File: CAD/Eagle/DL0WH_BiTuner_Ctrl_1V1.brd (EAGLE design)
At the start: 96.5 x 73 mm, 141 parts, among them Q0321 ABS07-32.768KHZ, U0101 STM32L476RXT_64PIN_LDO, U0601 MC33996, U0701 MC33996, U0801 MC33996, U0921 TS5A23166, U0951 OPA354, U1001 MAX232_SOIC16, U1101 MAX232_SOIC16, U1201 LM53603-Q1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

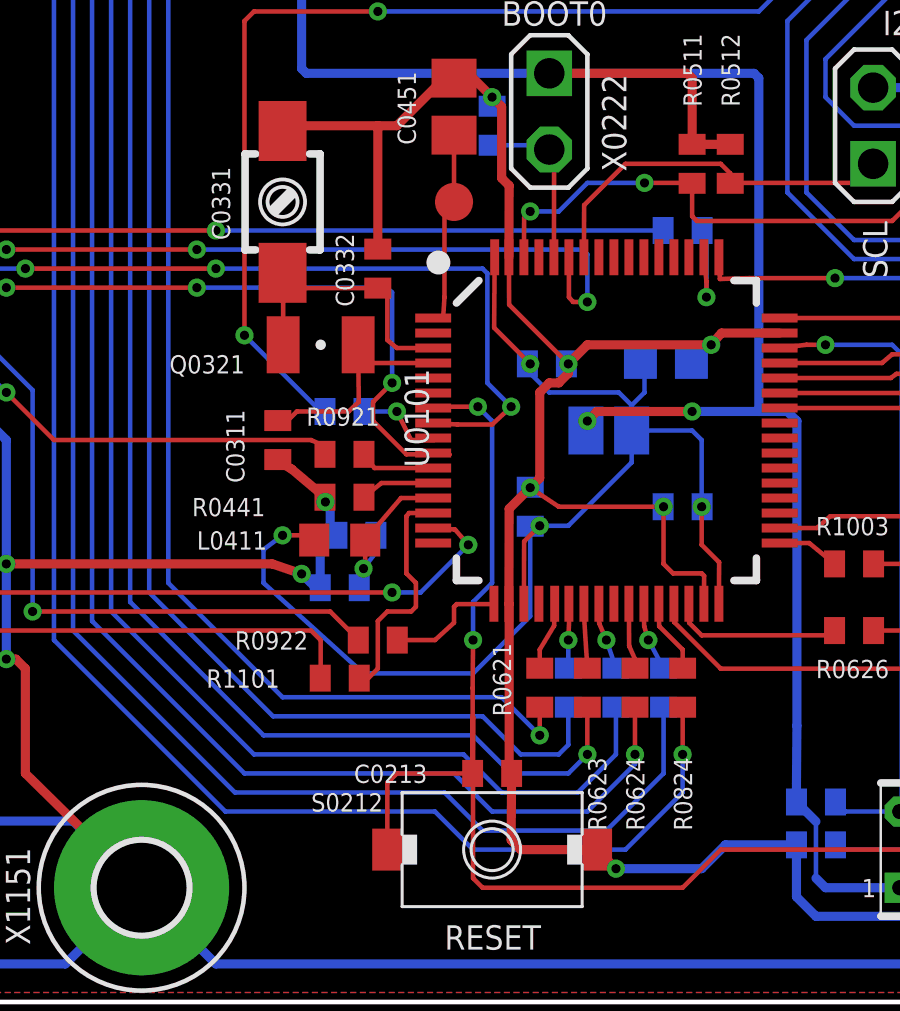
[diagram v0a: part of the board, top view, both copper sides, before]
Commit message: HW_1V1 - CAD/Eagle - after DRC fixes, ready for production with new STM32L476 device package.
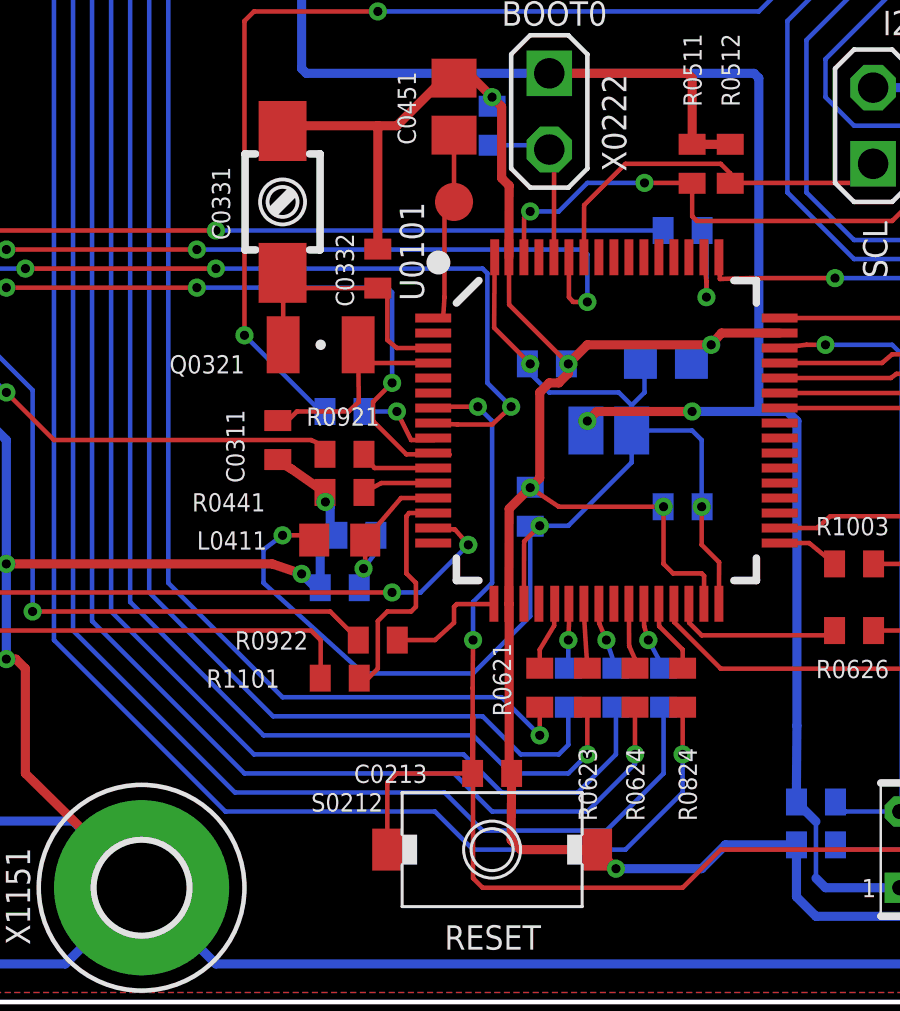
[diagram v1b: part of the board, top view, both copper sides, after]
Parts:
- moved R0441 0.16 mm to (59.8, 17.0)
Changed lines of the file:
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@@
 <layer number="37" name="tTest" color="7" fill="1" visible="no" active="yes"/>
 <layer number="38" name="bTest" color="7" fill="1" visible="no" active="yes"/>
-<layer number="39" name="tKeepout" color="4" fill="11" visible="no" active="yes"/>
-<layer number="40" name="bKeepout" color="1" fill="11" visible="no" active="yes"/>
-<layer number="41" name="tRestrict" color="4" fill="10" visible="no" active="yes"/>
-<layer number="42" name="bRestrict" color="1" fill="10" visible="no" active="yes"/>
-<layer number="43" name="vRestrict" color="2" fill="10" visible="no" active="yes"/>
+<layer number="39" name="tKeepout" color="4" fill="11" visible="yes" active="yes"/>
+<layer number="40" name="bKeepout" color="1" fill="11" visible="yes" active="yes"/>
+<layer number="41" name="tRestrict" color="4" fill="10" visible="yes" active="yes"/>
+<layer number="42" name="bRestrict" color="1" fill="10" visible="yes" active="yes"/>
+<layer number="43" name="vRestrict" color="2" fill="10" visible="yes" active="yes"/>
 <layer number="44" name="Drills" color="7" fill="1" visible="no" active="yes"/>
 <layer number="45" name="Holes" color="7" fill="1" visible="yes" active="yes"/>
@@
 <layer number="49" name="Reference" color="7" fill="1" visible="no" active="yes"/>
 <layer number="50" name="dxf" color="7" fill="1" visible="no" active="no"/>
-<layer number="51" name="tDocu" color="14" fill="1" visible="yes" active="yes"/>
-<layer number="52" name="bDocu" color="6" fill="1" visible="yes" active="yes"/>
+<layer number="51" name="tDocu" color="14" fill="1" visible="no" active="yes"/>
+<layer number="52" name="bDocu" color="6" fill="1" visible="no" active="yes"/>
 <layer number="53" name="tGND_GNDA" color="7" fill="9" visible="no" active="no"/>
 <layer number="54" name="bGND_GNDA" color="1" fill="9" visible="no" active="no"/>
@@
 <attribute name="VALUE" x="64.135" y="5.715" size="0.6096" layer="27" font="vector" ratio="10"/>
 </element>
-<element name="R0441" library="df4iah_rcl" package="R0402" value="0R" x="59.84875" y="16.8275" smashed="yes">
-<attribute name="NAME" x="54.76875" y="16.1925" size="0.6096" layer="25" font="vector" ratio="10"/>
-<attribute name="VALUE" x="59.21375" y="14.9225" size="0.6096" layer="27" font="vector" ratio="10"/>
+<element name="R0441" library="df4iah_rcl" package="R0402" value="0R" x="59.84875" y="16.98625" smashed="yes">
+<attribute name="NAME" x="54.76875" y="16.35125" size="0.6096" layer="25" font="vector" ratio="10"/>
+<attribute name="VALUE" x="59.21375" y="15.08125" size="0.6096" layer="27" font="vector" ratio="10"/>
 </element>
 <element name="C0451" library="df4iah_rcl" package="C0805" value="47uF" x="63.5" y="29.845" smashed="yes" rot="R90">
@@
 </element>
 <element name="U0101" library="df4iah_stm32l4" package="LQFP64" value="STM32L476RXT_64PIN_LDO" x="68.58" y="19.05" smashed="yes">
-<attribute name="NAME" x="62.6625" y="17.82125" size="0.8128" layer="25" rot="R90"/>
+<attribute name="NAME" x="62.50375" y="23.3775" size="0.8128" layer="25" rot="R90"/>
 <attribute name="VALUE" x="65.555" y="16.6" size="0.8128" layer="27"/>
 </element>
@@
 </element>
 <element name="R0622" library="df4iah_rcl" package="R0402" value="0R" x="67.31" y="10.4775" smashed="yes" rot="MR270">
-<attribute name="NAME" x="66.9925" y="5.715" size="0.6096" layer="26" font="vector" ratio="10" rot="MR90"/>
+<attribute name="NAME" x="66.83375" y="6.0325" size="0.6096" layer="26" font="vector" ratio="10" rot="MR90"/>
 <attribute name="VALUE" x="68.8975" y="12.065" size="0.6096" layer="28" font="vector" ratio="10" rot="MR270"/>
 </element>
 <element name="R0623" library="df4iah_rcl" package="R0402" value="47R" x="67.945" y="10.4775" smashed="yes" rot="R270">
-<attribute name="NAME" x="68.58" y="5.715" size="0.6096" layer="25" font="vector" ratio="10" rot="R90"/>
+<attribute name="NAME" x="68.2625" y="6.0325" size="0.6096" layer="25" font="vector" ratio="10" rot="R90"/>
 <attribute name="VALUE" x="66.3575" y="12.065" size="0.6096" layer="27" font="vector" ratio="10" rot="R270"/>
 </element>
 <element name="R0624" library="df4iah_rcl" package="R0402" value="47R" x="69.5325" y="10.4775" smashed="yes" rot="R270">
-<attribute name="NAME" x="69.85" y="5.715" size="0.6096" layer="25" font="vector" ratio="10" rot="R90"/>
+<attribute name="NAME" x="69.85" y="6.0325" size="0.6096" layer="25" font="vector" ratio="10" rot="R90"/>
 <attribute name="VALUE" x="67.945" y="12.065" size="0.6096" layer="27" font="vector" ratio="10" rot="R270"/>
 </element>
 <element name="R0625" library="df4iah_rcl" package="R0402" value="47R" x="68.8975" y="10.4775" smashed="yes" rot="MR270">
-<attribute name="NAME" x="68.58" y="5.715" size="0.6096" layer="26" font="vector" ratio="10" rot="MR90"/>
+<attribute name="NAME" x="68.58" y="6.0325" size="0.6096" layer="26" font="vector" ratio="10" rot="MR90"/>
 <attribute name="VALUE" x="70.485" y="12.065" size="0.6096" layer="28" font="vector" ratio="10" rot="MR270"/>
 </element>
@@
 </element>
 <element name="R0724" library="df4iah_rcl" package="R0402" value="47R" x="70.485" y="10.4775" smashed="yes" rot="MR270">
-<attribute name="NAME" x="70.1675" y="5.715" size="0.6096" layer="26" font="vector" ratio="10" rot="MR90"/>
+<attribute name="NAME" x="70.1675" y="6.0325" size="0.6096" layer="26" font="vector" ratio="10" rot="MR90"/>
 <attribute name="VALUE" x="72.0725" y="12.065" size="0.6096" layer="28" font="vector" ratio="10" rot="MR270"/>
 </element>
 <element name="R0824" library="df4iah_rcl" package="R0402" value="47R" x="71.12" y="10.4775" smashed="yes" rot="R270">
-<attribute name="NAME" x="71.4375" y="5.715" size="0.6096" layer="25" font="vector" ratio="10" rot="R90"/>
+<attribute name="NAME" x="71.59625" y="6.0325" size="0.6096" layer="25" font="vector" ratio="10" rot="R90"/>
 <attribute name="VALUE" x="69.5325" y="12.065" size="0.6096" layer="27" font="vector" ratio="10" rot="R270"/>
 </element>
@@
 <wire x1="65.3375" y1="13.2675" x2="65.3375" y2="7.855" width="0.3048" layer="1"/>
 <wire x1="65.3375" y1="7.855" x2="65.42" y2="7.62" width="0.3048" layer="1"/>
-<wire x1="59.19875" y1="16.8275" x2="58.0875" y2="17.765" width="0.3048" layer="1"/>
+<wire x1="59.19875" y1="16.98625" x2="58.0875" y2="17.765" width="0.3048" layer="1"/>
 <wire x1="58.0875" y1="17.765" x2="57.785" y2="17.93875" width="0.3048" layer="1"/>
 <wire x1="57.785" y1="17.93875" x2="57.61125" y2="18.0975" width="0.1524" layer="1"/>
@@
 <wire x1="67.945" y1="21.9075" x2="72.0725" y2="21.9075" width="0.3048" layer="1"/>
 <via x="59.21375" y="16.66875" extent="1-16" drill="0.3048"/>
-<wire x1="59.19875" y1="16.8275" x2="59.055" y2="16.66875" width="0.1524" layer="1"/>
+<wire x1="59.19875" y1="16.98625" x2="59.055" y2="16.66875" width="0.1524" layer="1"/>
 <wire x1="59.055" y1="16.66875" x2="59.21375" y2="16.66875" width="0.3048" layer="1"/>
 <wire x1="59.595625" y1="15.5575" x2="59.3725" y2="15.5575" width="0.3048" layer="16"/>
@@
 <contactref element="U0101" pad="12"/>
 <wire x1="62.805" y1="17.3" x2="61.08" y2="17.3" width="0.1524" layer="1"/>
-<wire x1="61.08" y1="17.3" x2="60.49875" y2="16.8275" width="0.1524" layer="1"/>
+<wire x1="61.08" y1="17.3" x2="60.49875" y2="16.98625" width="0.1524" layer="1"/>
 </signal>
 <signal name="PH3_BOOT0">

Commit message: HW_1V0 HW_1V1 HW_1V2 - TPS62051 changed to TPS62056
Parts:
- U1301: value TPS62051 -> TPS62056
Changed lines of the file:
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@@
 <attribute name="VALUE" x="69.5325" y="12.065" size="0.6096" layer="27" font="vector" ratio="10" rot="R270"/>
 </element>
-<element name="U1301" library="df4iah_powersupply" package="S-PDSO-G10" value="TPS62051" x="15.24" y="39.37" rot="R180"/>
+<element name="U1301" library="df4iah_powersupply" package="S-PDSO-G10" value="TPS62056" x="15.24" y="39.37" rot="R180"/>
 <element name="L1311" library="df4iah_rcl" package="L_4.50MM_X_3.20MM" value="10uH" x="21.9075" y="36.83" smashed="yes" rot="R180">
 <attribute name="NAME" x="20.6375" y="38.735" size="0.6096" layer="25" font="vector" ratio="10"/>
